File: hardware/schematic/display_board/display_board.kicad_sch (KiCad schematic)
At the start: 7 parts, among them J1 Conn_01x04_Pin, SW1 SW_Push, SW2 SW_Push

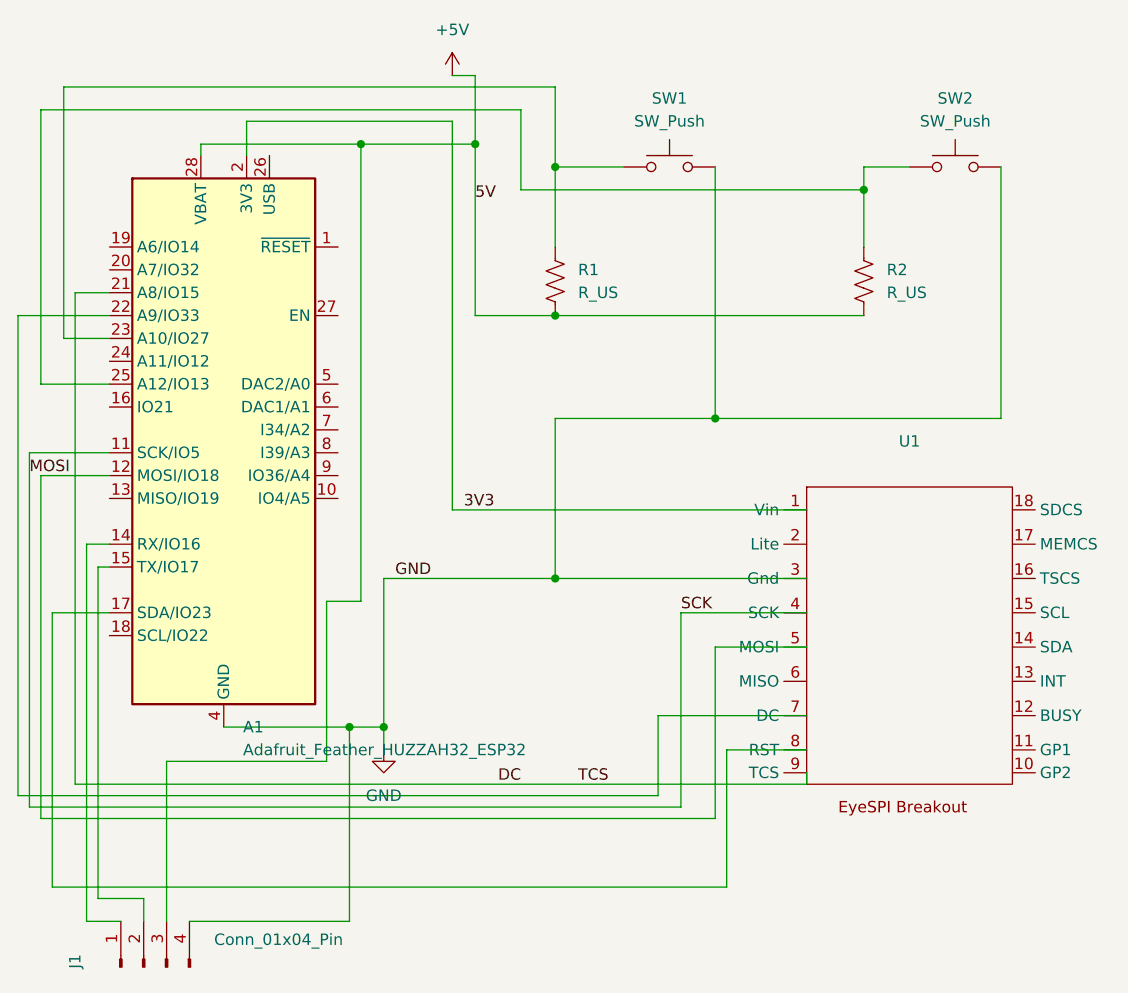
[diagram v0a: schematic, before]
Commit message: Consolidate display_board/nav_board KiCad files to latest local work
This machine has the most recent hardware design work. Promote the
Rev B design to canonical display_board.kicad_pro/.kicad_sch/.kicad_pcb,
move its matching gerbers/drill files into manufacturing/, track the
gopro-housing variant as a maintained alternate board, and drop the
superseded Rev A files, stale fabrication/ output, and backup zips
(archived locally under a gitignored _archive/ folder rather than
deleted outright). Also brings nav_board's schematic/PCB/manufacturing
files up to date.

Co-Authored-By: Claude Sonnet 5 <noreply@anthropic.com>
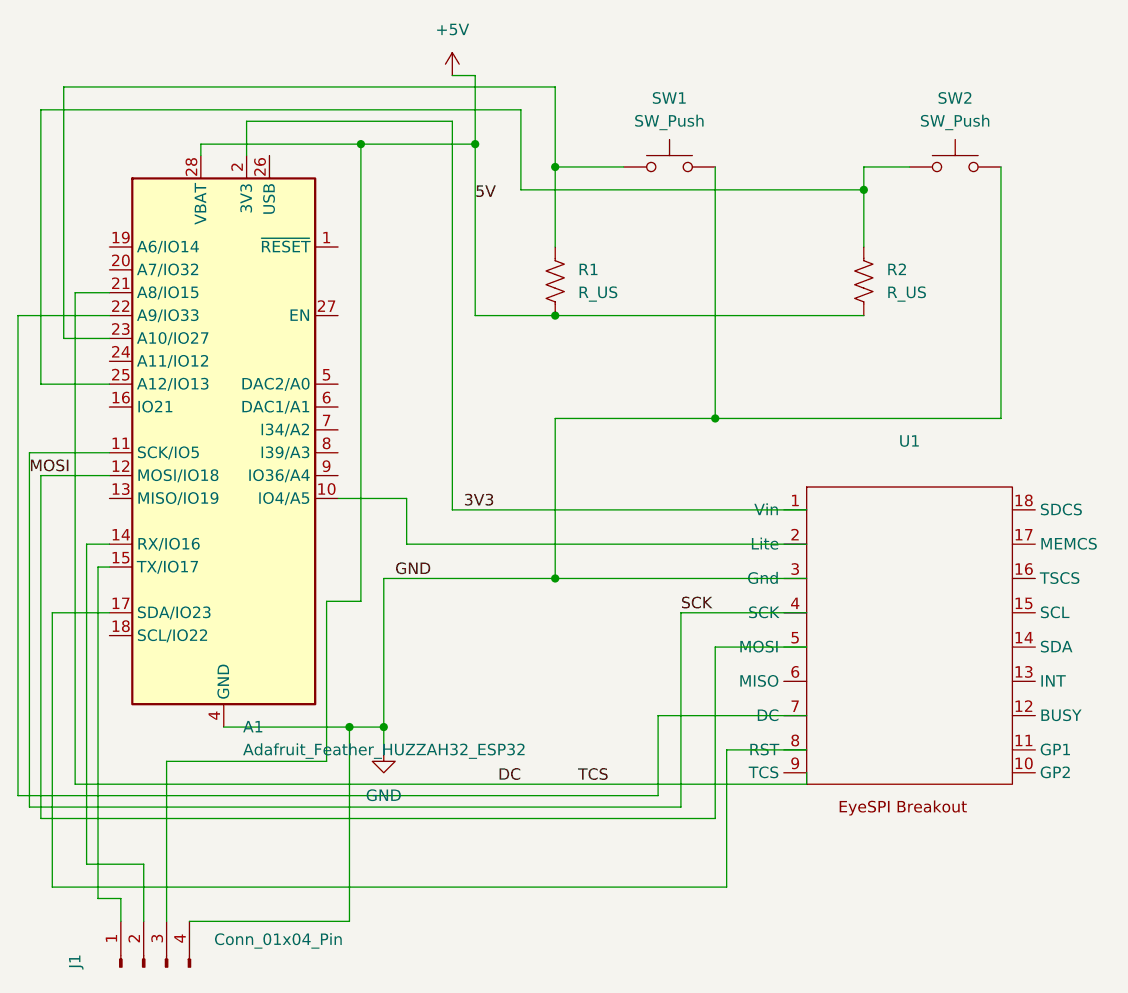
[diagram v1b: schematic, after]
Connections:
- net at A1.10 (IO4/A5): now also U1.2 (Lite)
- net at A1.14 (RX/IO16): now also J1.2 (Pin_2); no longer J1.1 (Pin_1)
- net at A1.15 (TX/IO17): now also J1.1 (Pin_1); no longer J1.2 (Pin_2)
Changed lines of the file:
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@@
+	(wire
+		(pts
+			(xy 31.75 113.03) (xy 34.29 113.03)
+		)
+		(stroke
+			(width 0)
+			(type default)
+		)
+	)
 	(wire
 		(pts
@@
 	(wire
 		(pts
+			(xy 34.29 113.03) (xy 34.29 115.57)
+		)
+		(stroke
+			(width 0)
+			(type default)
+		)
+	)
+	(wire
+		(pts
 			(xy 48.26 30.48) (xy 48.26 26.67)
 		)
@@
 	(wire
 		(pts
+			(xy 66.04 73.66) (xy 110.49 73.66)
+		)
+		(stroke
+			(width 0)
+			(type default)
+		)
+	)
+	(wire
+		(pts
 			(xy 71.12 26.67) (xy 71.12 69.85)
 		)
@@
 	(wire
 		(pts
-			(xy 34.29 115.57) (xy 30.48 115.57)
-		)
-		(stroke
-			(width 0)
-			(type default)
-		)
-	)
-	(wire
-		(pts
-			(xy 30.48 115.57) (xy 30.48 73.66)
-		)
-		(stroke
-			(width 0)
-			(type default)
-		)
-	)
-	(wire
-		(pts
 			(xy 110.49 77.47) (xy 82.55 77.47)
 		)
@@
 	(wire
 		(pts
+			(xy 66.04 68.58) (xy 66.04 73.66)
+		)
+		(stroke
+			(width 0)
+			(type default)
+		)
+	)
+	(wire
+		(pts
+			(xy 30.48 109.22) (xy 30.48 73.66)
+		)
+		(stroke
+			(width 0)
+			(type default)
+		)
+	)
+	(wire
+		(pts
 			(xy 33.02 81.28) (xy 26.67 81.28)
 		)
@@
 	(wire
 		(pts
-			(xy 36.83 113.03) (xy 36.83 115.57)
-		)
-		(stroke
-			(width 0)
-			(type default)
-		)
-	)
-	(wire
-		(pts
 			(xy 24.13 63.5) (xy 24.13 102.87)
 		)
@@
 	(wire
 		(pts
+			(xy 30.48 109.22) (xy 36.83 109.22)
+		)
+		(stroke
+			(width 0)
+			(type default)
+		)
+	)
+	(wire
+		(pts
 			(xy 48.26 26.67) (xy 71.12 26.67)
 		)
@@
 	(wire
 		(pts
-			(xy 31.75 113.03) (xy 36.83 113.03)
-		)
-		(stroke
-			(width 0)
-			(type default)
-		)
-	)
-	(wire
-		(pts
 			(xy 101.6 96.52) (xy 110.49 96.52)
 		)
@@
 		)
 		(stroke
+			(width 0)
+			(type default)
+		)
+	)
+	(wire
+		(pts
+			(xy 58.42 68.58) (xy 66.04 68.58)
+		)
+		(stroke
+			(width 0)
+			(type default)
+		)
+	)
+	(wire
+		(pts
+			(xy 36.83 115.57) (xy 36.83 109.22)
+		)
+		(stroke
